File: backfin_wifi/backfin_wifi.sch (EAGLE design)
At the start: 28 parts, among them SW1 SPST_TACT-EVQQ2

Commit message: Initial placement complete...
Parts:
- removed U$6: 0OHM_JMPR, custom:0OHM_JMPR
- added C7, C8: 1uF, rcl:C-EUC0402K
- added R6: 0, resistor:R-US_R1005
- added R7: NL, resistor:R-US_R1005
- TP1, TP2, TP3, TP4, TP5: value TPPAD1-13 -> TPB1,27; device testpad:TPPAD1-13 -> testpad:TPB1,27
- renumbered U$1 to U1, U$3 to ANT1, U$4 to L1, U$5 to L2, U$7 to U7, U$8 to U8
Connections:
- removed net N$14 (its old number): U8.B4
- new net +3V3: U$2.3V
- new net +5V: C5.1, C8.2, J1.2, R4.1, U$2.5V, U7.EN, U7.IN, U8.VCCB
- net GND: now also C7.1, C8.1, Q1.S, R7.2; no longer Q1.D
- net N$1: now also R6.1
- net N$2: now also R6.2, R7.1
- net N$20: now also Q1.D; no longer Q1.S
- net SPI_CLK_HOST: no longer U$2.D13
- net SPI_CS_HOST: now also U8.B1; no longer U8.B6
- net SPI_DIN_HOST: no longer U$2.D11
- net SPI_DOUT_HOST: no longer U$2.D12
- net SPI_IRQ_HOST: now also U8.B4
- net VBAT_SW_EN: now also U8.B6; no longer U8.B1
- net VCC: now also C7.2; no longer C5.1, J1.2, R4.1, U$2.3V, U$2.5V, U7.EN, U7.IN, U8.VCCB
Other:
- moved on the sheet: Q1, R5

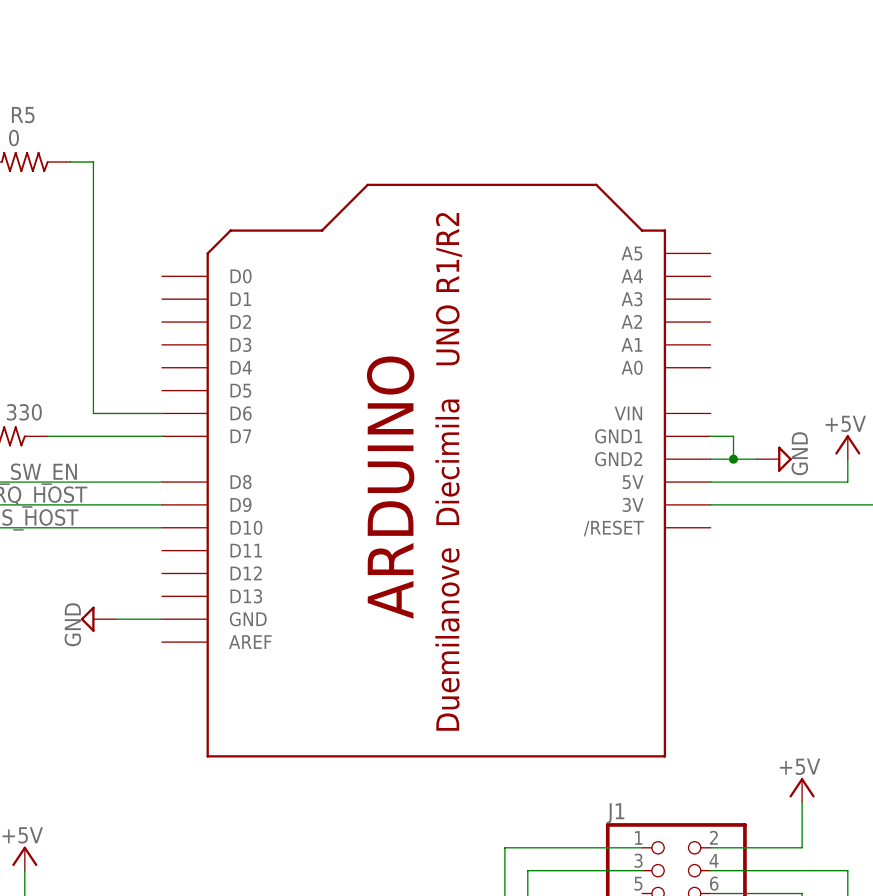
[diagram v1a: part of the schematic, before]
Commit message: Only transmission line remains...
Contacted 4PCB to see what their $33 standard stackup is.
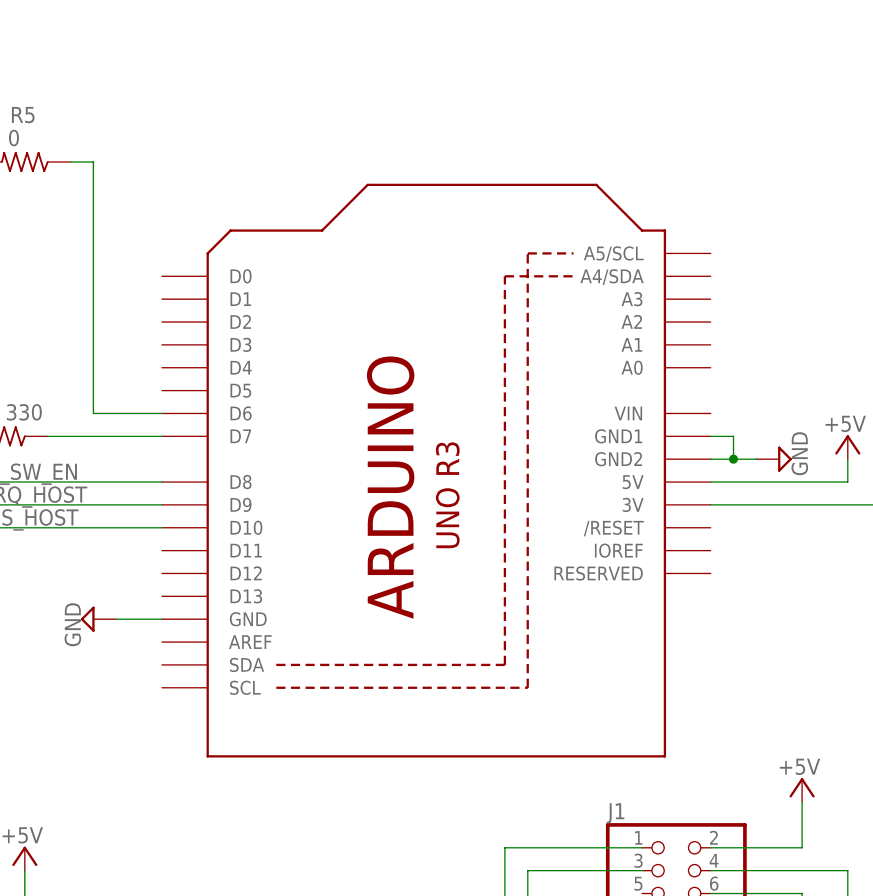
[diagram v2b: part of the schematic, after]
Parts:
- removed U$2: ARDUINOUNO, adafruit:ARDUINOUNO
- added U2: ARDUINOR3-DIMENSION, custom:ARDUINOR3-DIMENSION
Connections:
- net +3V3: now also U2.3V; no longer U$2.3V
- net +5V: now also U2.5V; no longer U$2.5V
- net GND: now also U2.GND, U2.GND1, U2.GND2; no longer U$2.GND, U$2.GND1, U$2.GND2
- net N$17: now also U2.D7; no longer U$2.D7
- net N$19: now also U2.D6; no longer U$2.D6
- net SPI_CS_HOST: now also U2.D10; no longer U$2.D10
- net SPI_IRQ_HOST: now also U2.D9; no longer U$2.D9
- net VBAT_SW_EN: now also U2.D8; no longer U$2.D8

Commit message: Worked on library code.
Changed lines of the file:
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@@
 <grid distance="0.1" unitdist="inch" unit="inch" style="lines" multiple="1" display="no" altdistance="0.01" altunitdist="inch" altunit="inch"/>
 <layers>
-<layer number="1" name="Top" color="4" fill="1" visible="no" active="no"/>
-<layer number="2" name="Route2" color="1" fill="3" visible="no" active="no"/>
-<layer number="3" name="Route3" color="4" fill="3" visible="no" active="no"/>
-<layer number="4" name="Route4" color="1" fill="4" visible="no" active="no"/>
-<layer number="5" name="Route5" color="4" fill="4" visible="no" active="no"/>
-<layer number="6" name="Route6" color="1" fill="8" visible="no" active="no"/>
-<layer number="7" name="Route7" color="4" fill="8" visible="no" active="no"/>
-<layer number="8" name="Route8" color="1" fill="2" visible="no" active="no"/>
-<layer number="9" name="Route9" color="4" fill="2" visible="no" active="no"/>
-<layer number="10" name="Route10" color="1" fill="7" visible="no" active="no"/>
-<layer number="11" name="Route11" color="4" fill="7" visible="no" active="no"/>
-<layer number="12" name="Route12" color="1" fill="5" visible="no" active="no"/>
-<layer number="13" name="Route13" color="4" fill="5" visible="no" active="no"/>
-<layer number="14" name="Route14" color="1" fill="6" visible="no" active="no"/>
-<layer number="15" name="Route15" color="4" fill="6" visible="no" active="no"/>
-<layer number="16" name="Bottom" color="1" fill="1" visible="no" active="no"/>
-<layer number="17" name="Pads" color="2" fill="1" visible="no" active="no"/>
-<layer number="18" name="Vias" color="2" fill="1" visible="no" active="no"/>
-<layer number="19" name="Unrouted" color="6" fill="1" visible="no" active="no"/>
-<layer number="20" name="Dimension" color="15" fill="1" visible="no" active="no"/>
-<layer number="21" name="tPlace" color="7" fill="1" visible="no" active="no"/>
-<layer number="22" name="bPlace" color="7" fill="1" visible="no" active="no"/>
-<layer number="23" name="tOrigins" color="15" fill="1" visible="no" active="no"/>
-<layer number="24" name="bOrigins" color="15" fill="1" visible="no" active="no"/>
-<layer number="25" name="tNames" color="7" fill="1" visible="no" active="no"/>
-<layer number="26" name="bNames" color="7" fill="1" visible="no" active="no"/>
-<layer number="27" name="tValues" color="7" fill="1" visible="no" active="no"/>
-<layer number="28" name="bValues" color="7" fill="1" visible="no" active="no"/>
+<layer number="1" name="Top" color="4" fill="1" visible="yes" active="no"/>
+<layer number="2" name="Route2" color="1" fill="3" visible="yes" active="no"/>
+<layer number="3" name="Route3" color="4" fill="3" visible="yes" active="no"/>
+<layer number="4" name="Route4" color="1" fill="4" visible="yes" active="no"/>
+<layer number="5" name="Route5" color="4" fill="4" visible="yes" active="no"/>
+<layer number="6" name="Route6" color="1" fill="8" visible="yes" active="no"/>
+<layer number="7" name="Route7" color="4" fill="8" visible="yes" active="no"/>
+<layer number="8" name="Route8" color="1" fill="2" visible="yes" active="no"/>
+<layer number="9" name="Route9" color="4" fill="2" visible="yes" active="no"/>
+<layer number="10" name="Route10" color="1" fill="7" visible="yes" active="no"/>
+<layer number="11" name="Route11" color="4" fill="7" visible="yes" active="no"/>
+<layer number="12" name="Route12" color="1" fill="5" visible="yes" active="no"/>
+<layer number="13" name="Route13" color="4" fill="5" visible="yes" active="no"/>
+<layer number="14" name="Route14" color="1" fill="6" visible="yes" active="no"/>
+<layer number="15" name="Route15" color="4" fill="6" visible="yes" active="no"/>
+<layer number="16" name="Bottom" color="1" fill="1" visible="yes" active="no"/>
+<layer number="17" name="Pads" color="2" fill="1" visible="yes" active="no"/>
+<layer number="18" name="Vias" color="2" fill="1" visible="yes" active="no"/>
+<layer number="19" name="Unrouted" color="6" fill="1" visible="yes" active="no"/>
+<layer number="20" name="Dimension" color="15" fill="1" visible="yes" active="no"/>
+<layer number="21" name="tPlace" color="7" fill="1" visible="yes" active="no"/>
+<layer number="22" name="bPlace" color="7" fill="1" visible="yes" active="no"/>
+<layer number="23" name="tOrigins" color="15" fill="1" visible="yes" active="no"/>
+<layer number="24" name="bOrigins" color="15" fill="1" visible="yes" active="no"/>
+<layer number="25" name="tNames" color="7" fill="1" visible="yes" active="no"/>
+<layer number="26" name="bNames" color="7" fill="1" visible="yes" active="no"/>
+<layer number="27" name="tValues" color="7" fill="1" visible="yes" active="no"/>
+<layer number="28" name="bValues" color="7" fill="1" visible="yes" active="no"/>
 <layer number="29" name="tStop" color="7" fill="3" visible="no" active="no"/>
 <layer number="30" name="bStop" color="7" fill="6" visible="no" active="no"/>
@@
 <layer number="35" name="tGlue" color="7" fill="4" visible="no" active="no"/>
 <layer number="36" name="bGlue" color="7" fill="5" visible="no" active="no"/>
-<layer number="37" name="tTest" color="7" fill="1" visible="no" active="no"/>
-<layer number="38" name="bTest" color="7" fill="1" visible="no" active="no"/>
+<layer number="37" name="tTest" color="7" fill="1" visible="yes" active="no"/>
+<layer number="38" name="bTest" color="7" fill="1" visible="yes" active="no"/>
 <layer number="39" name="tKeepout" color="4" fill="11" visible="no" active="no"/>
 <layer number="40" name="bKeepout" color="1" fill="11" visible="no" active="no"/>
@@
 <layer number="44" name="Drills" color="7" fill="1" visible="no" active="no"/>
 <layer number="45" name="Holes" color="7" fill="1" visible="no" active="no"/>
-<layer number="46" name="Milling" color="3" fill="1" visible="no" active="no"/>
-<layer number="47" name="Measures" color="7" fill="1" visible="no" active="no"/>
-<layer number="48" name="Document" color="7" fill="1" visible="no" active="no"/>
-<layer number="49" name="Reference" color="7" fill="1" visible="no" active="no"/>
-<layer number="50" name="dxf" color="7" fill="1" visible="no" active="no"/>
-<layer number="51" name="tDocu" color="7" fill="1" visible="no" active="no"/>
-<layer number="52" name="bDocu" color="7" fill="1" visible="no" active="no"/>
-<layer number="53" name="tGND_GNDA" color="7" fill="9" visible="no" active="no"/>
-<layer number="54" name="bGND_GNDA" color="1" fill="9" visible="no" active="no"/>
-<layer number="56" name="wert" color="7" fill="1" visible="no" active="no"/>
+<layer number="46" name="Milling" color="3" fill="1" visible="yes" active="no"/>
+<layer number="47" name="Measures" color="7" fill="1" visible="yes" active="no"/>
+<layer number="48" name="Document" color="7" fill="1" visible="yes" active="no"/>
+<layer number="49" name="Reference" color="7" fill="1" visible="yes" active="no"/>
+<layer number="50" name="dxf" color="7" fill="1" visible="yes" active="no"/>
+<layer number="51" name="tDocu" color="7" fill="1" visible="yes" active="no"/>
+<layer number="52" name="bDocu" color="7" fill="1" visible="yes" active="no"/>
+<layer number="53" name="tGND_GNDA" color="7" fill="9" visible="yes" active="no"/>
+<layer number="54" name="bGND_GNDA" color="1" fill="9" visible="yes" active="no"/>
+<layer number="56" name="wert" color="7" fill="1" visible="yes" active="no"/>
 <layer number="91" name="Nets" color="2" fill="1" visible="yes" active="yes"/>
 <layer number="92" name="Busses" color="1" fill="1" visible="yes" active="yes"/>
@@
 <pinref part="U1" gate="G$1" pin="GND18"/>
 <wire x1="38.1" y1="-22.86" x2="38.1" y2="-27.94" width="0.1524" layer="91"/>
+<junction x="30.48" y="-27.94"/>
+<junction x="33.02" y="-27.94"/>
+<junction x="35.56" y="-27.94"/>
 </segment>
 <segment>
@@
 </sheet>
 </sheets>
+<errors>
+</errors>
 </schematic>
 </drawing>
